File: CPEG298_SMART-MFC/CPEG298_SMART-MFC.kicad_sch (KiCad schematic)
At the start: 4 parts, among them J1 Power, J2 Digital/PWM, J3 Analog, J4 Digital/PWM

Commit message: Lab4_Complete
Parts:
- added C1: C_Polarized_US, Capacitor_THT:CP_Radial_D6.3mm_P2.50mm, symbol Device:C_Polarized_US
- added R1: 1000, Resistor_THT:R_Axial_DIN0207_L6.3mm_D2.5mm_P10.16mm_Horizontal, symbol Device:R_US
- added R2: 2000, Resistor_THT:R_Axial_DIN0207_L6.3mm_D2.5mm_P10.16mm_Horizontal, symbol Device:R_US
- added U1: ESP8266-01/ESP-01, ESP8266-01_ESP-01:XCVR_ESP8266-01_ESP-01, symbol ESP8266-01_ESP-01:ESP8266-01/ESP-01
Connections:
- net *10: now also U1.5 (TXD)
- net *11: now also R1.1
- net +5V: now also C1.1
- net GND: now also C1.2, R2.2, U1.1 (GND)
- new net: R1.2, R2.1, U1.4 (RXD)
- new net +3.3V: U1.6 (EN), U1.8 (VCC)

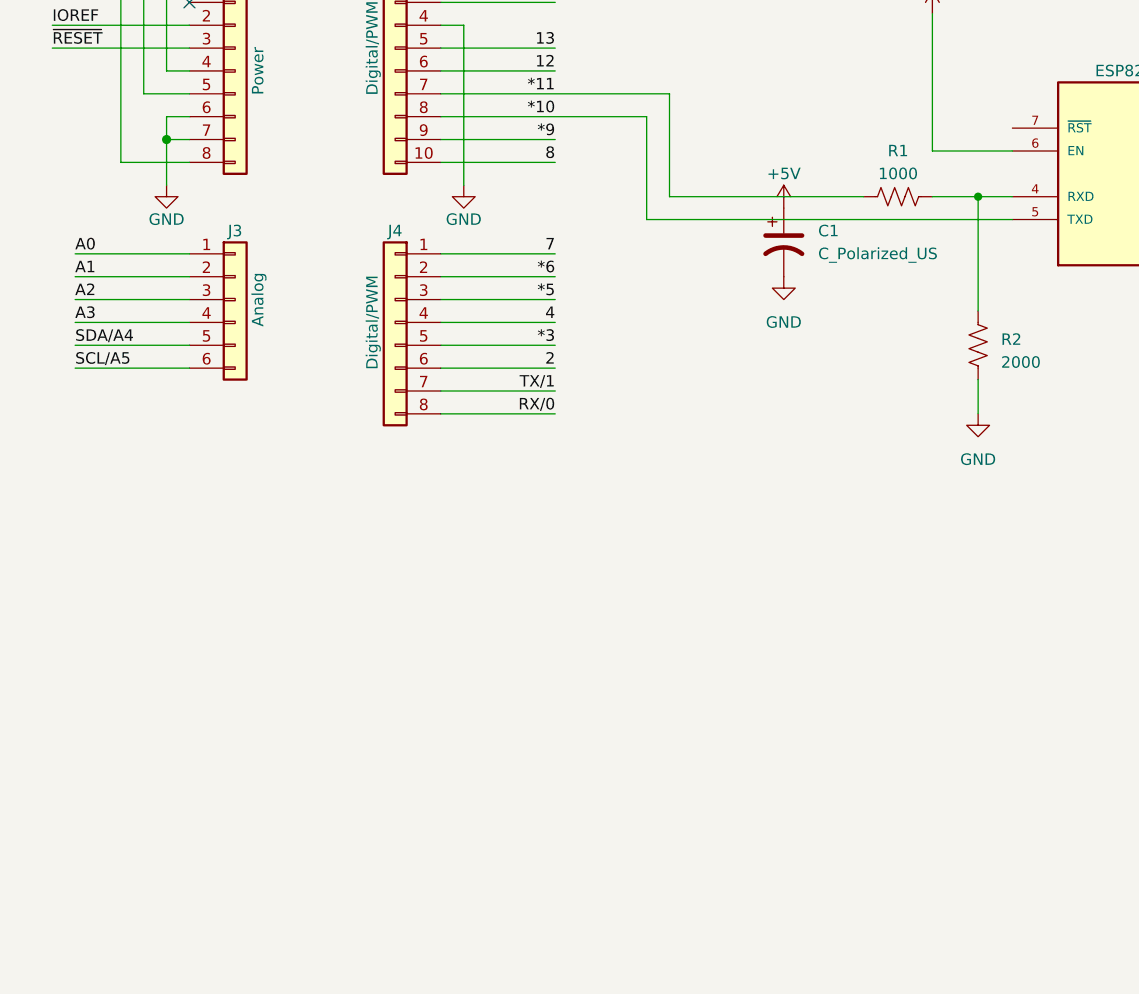
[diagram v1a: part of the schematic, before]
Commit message: Lab5
-Added Grove Connectors
-Rewiring
-3D STEP Files
-New Libraries
*SEEED, Digikey
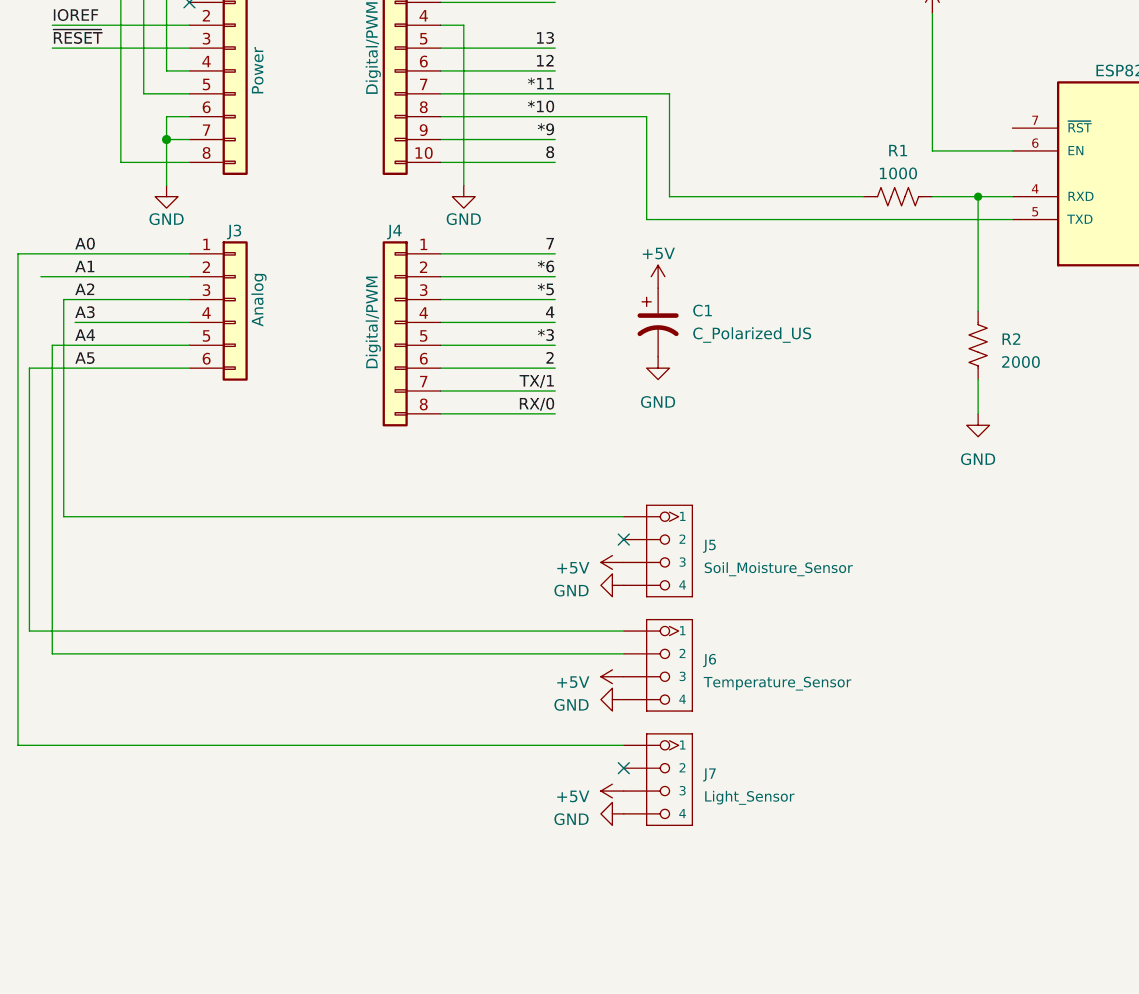
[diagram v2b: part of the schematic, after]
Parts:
- added J5: Soil_Moisture_Sensor, OPL_Connector:HW4-2.0, symbol OPL_Connector:GROVE-CONNECTOR-DIP_4P-2.0_
- added J6: Temperature_Sensor, OPL_Connector:HW4-2.0, symbol OPL_Connector:GROVE-CONNECTOR-DIP_4P-2.0_
- added J7: Light_Sensor, OPL_Connector:HW4-2.0, symbol OPL_Connector:GROVE-CONNECTOR-DIP_4P-2.0_
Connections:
- net +5V: now also J5.3, J6.3, J7.3
- net A0: now also J7.1
- net A2: now also J5.1
- net GND: now also J5.4, J6.4, J7.4
- net SCL/A5: no longer J3.6 (Pin_6)
- net SDA/A4: no longer J3.5 (Pin_5)
- new net A4: J3.5 (Pin_5), J6.2
- new net A5: J3.6 (Pin_6), J6.1
- no-connect marks 1 -> 3
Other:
- moved on the sheet: C1

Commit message: KiCad Components and Software
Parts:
- added C2: C_Polarized_US, Capacitor_THT:CP_Radial_D6.3mm_P2.50mm, symbol Device:C_Polarized_US
- added D1: Soil Moisture Threshold, LED_THT:LED_D5.0mm, symbol Device:LED
- added J8: LCD, OPL_Connector:HW4-2.0, symbol OPL_Connector:GROVE-CONNECTOR-DIP_4P-2.0_
- added R3: R, Resistor_THT:R_Axial_DIN0207_L6.3mm_D2.5mm_P10.16mm_Horizontal, symbol Device:R_US
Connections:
- net +3.3V: now also C2.1
- net +5V: now also J8.3
- net 7: now also R3.1
- net GND: now also C2.2, D1.2 (A), J8.4
- net SCL/A5: now also J8.1
- net SDA/A4: now also J8.2
- new net: D1.1 (K), R3.2
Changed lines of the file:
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@@
     (stroke (width 0) (type solid))
   )
-  (wire (pts (xy 62.23 26.67) (xy 74.93 26.67))
+  (wire (pts (xy 62.23 26.67) (xy 92.71 26.67))
     (stroke (width 0) (type solid))
   )
@@
     (stroke (width 0) (type solid))
   )
+  (wire (pts (xy 82.55 59.69) (xy 82.55 86.36))
+    (stroke (width 0) (type default))
+  )
   (wire (pts (xy 62.23 36.83) (xy 74.93 36.83))
     (stroke (width 0) (type solid))
@@
     (stroke (width 0) (type solid))
   )
-  (wire (pts (xy 62.23 59.69) (xy 74.93 59.69))
+  (wire (pts (xy 62.23 59.69) (xy 82.55 59.69))
     (stroke (width 0) (type solid))
   )
@@
     (stroke (width 0) (type default))
   )
+  (wire (pts (xy 82.55 86.36) (xy 135.89 86.36))
+    (stroke (width 0) (type default))
+  )
   (wire (pts (xy 161.29 58.42) (xy 168.91 58.42))
     (stroke (width 0) (type default))
   )
-  (wire (pts (xy 62.23 29.21) (xy 74.93 29.21))
+  (wire (pts (xy 62.23 29.21) (xy 92.71 29.21))
     (stroke (width 0) (type solid))
   )
@@
     )
   )
+  (symbol (lib_name "+5V_1") (lib_id "power:+5V") (at 92.71 31.75 90) (unit 1)
+    (in_bom yes) (on_board yes) (dnp no) (fields_autoplaced)
+    (property "Reference" "#PWR022" (at 96.52 31.75 0)
+      (effects (font (size 1.27 1.27)) hide)
+    )
+    (property "Value" "+5V" (at 88.9 32.385 90)
+      (effects (font (size 1.27 1.27)) (justify left))
+    )
+    (property "Footprint" "" (at 92.71 31.75 0)
+      (effects (font (size 1.27 1.27)) hide)
+    )
+    (property "Datasheet" "" (at 92.71 31.75 0)
+      (effects (font (size 1.27 1.27)) hide)
+    )
+    (pin "1")
+    (instances
+      (project "CPEG298_SMART-MFC"
+        (path "/e63e39d7-6ac0-4ffd-8aa3-1841a4541b55"
+          (reference "#PWR022") (unit 1)
+        )
+      )
+    )
+  )
   (symbol (lib_id "OPL_Connector:GROVE-CONNECTOR-DIP_4P-2.0_") (at 86.36 118.11 0) (unit 1)
     (in_bom yes) (on_board yes) (dnp no) (fields_autoplaced)
@@
         (path "/e63e39d7-6ac0-4ffd-8aa3-1841a4541b55"
           (reference "J7") (unit 1)
+        )
+      )
+    )
+  )
+  (symbol (lib_name "GND_3") (lib_id "power:GND") (at 135.89 101.6 0) (unit 1)
+    (in_bom yes) (on_board yes) (dnp no) (fields_autoplaced)
+    (property "Reference" "#PWR020" (at 135.89 107.95 0)
+      (effects (font (size 1.27 1.27)) hide)
+    )
+    (property "Value" "GND" (at 135.89 106.68 0)
+      (effects (font (size 1.27 1.27)))
+    )
+    (property "Footprint" "" (at 135.89 101.6 0)
+      (effects (font (size 1.27 1.27)) hide)
+    )
+    (property "Datasheet" "" (at 135.89 101.6 0)
+      (effects (font (size 1.27 1.27)) hide)
+    )
+    (pin "1")
+    (instances
+      (project "CPEG298_SMART-MFC"
+        (path "/e63e39d7-6ac0-4ffd-8aa3-1841a4541b55"
+          (reference "#PWR020") (unit 1)
+        )
+      )
+    )
+  )
+  (symbol (lib_id "OPL_Connector:GROVE-CONNECTOR-DIP_4P-2.0_") (at 96.52 30.48 0) (unit 1)
+    (in_bom yes) (on_board yes) (dnp no) (fields_autoplaced)
+    (property "Reference" "J8" (at 101.6 29.845 0)
+      (effects (font (size 1.143 1.143)) (justify left))
+    )
+    (property "Value" "LCD" (at 101.6 32.385 0)
+      (effects (font (size 1.143 1.143)) (justify left))
+    )
+    (property "Footprint" "OPL_Connector:HW4-2.0" (at 96.52 30.48 0)
+      (effects (font (size 1.27 1.27)) hide)
+    )
+    (property "Datasheet" "" (at 96.52 30.48 0)
+      (effects (font (size 1.27 1.27)) hide)
+    )
+    (property "SKU" "320110033" (at 97.282 26.67 0)
+      (effects (font (size 0.508 0.508)) hide)
+    )
+    (pin "1")
+    (pin "2")
+    (pin "3")
+    (pin "4")
+    (instances
+      (project "CPEG298_SMART-MFC"
+        (path "/e63e39d7-6ac0-4ffd-8aa3-1841a4541b55"
+          (reference "J8") (unit 1)
+        )
+      )
+    )
+  )
+  (symbol (lib_name "GND_1") (lib_id "power:GND") (at 107.95 72.39 0) (unit 1)
+    (in_bom yes) (on_board yes) (dnp no) (fields_autoplaced)
+    (property "Reference" "#PWR019" (at 107.95 78.74 0)
+      (effects (font (size 1.27 1.27)) hide)
+    )
+    (property "Value" "GND" (at 107.95 77.47 0)
+      (effects (font (size 1.27 1.27)))
+    )
+    (property "Footprint" "" (at 107.95 72.39 0)
+      (effects (font (size 1.27 1.27)) hide)
+    )
+    (property "Datasheet" "" (at 107.95 72.39 0)
+      (effects (font (size 1.27 1.27)) hide)
+    )
+    (pin "1")
+    (instances
+      (project "CPEG298_SMART-MFC"
+        (path "/e63e39d7-6ac0-4ffd-8aa3-1841a4541b55"
+          (reference "#PWR019") (unit 1)
         )
       )
@@
     )
   )
+  (symbol (lib_id "power:+3.3V") (at 107.95 64.77 0) (unit 1)
+    (in_bom yes) (on_board yes) (dnp no) (fields_autoplaced)
+    (property "Reference" "#PWR018" (at 107.95 68.58 0)
+      (effects (font (size 1.27 1.27)) hide)
+    )
+    (property "Value" "+3.3V" (at 107.95 60.96 0)
+      (effects (font (size 1.27 1.27)))
+    )
+    (property "Footprint" "" (at 107.95 64.77 0)
+      (effects (font (size 1.27 1.27)) hide)
+    )
+    (property "Datasheet" "" (at 107.95 64.77 0)
+      (effects (font (size 1.27 1.27)) hide)
+    )
+    (pin "1")
+    (instances
+      (project "CPEG298_SMART-MFC"
+        (path "/e63e39d7-6ac0-4ffd-8aa3-1841a4541b55"
+          (reference "#PWR018") (unit 1)
+        )
+      )
+    )
+  )
   (symbol (lib_name "GND_2") (lib_id "power:GND") (at 168.91 67.31 0) (unit 1)
     (in_bom yes) (on_board yes) (dnp no) (fields_autoplaced)
@@
         (path "/e63e39d7-6ac0-4ffd-8aa3-1841a4541b55"
           (reference "#PWR010") (unit 1)
+        )
+      )
+    )
+  )
+  (symbol (lib_name "GND_1") (lib_id "power:GND") (at 92.71 34.29 270) (unit 1)
+    (in_bom yes) (on_board yes) (dnp no) (fields_autoplaced)
+    (property "Reference" "#PWR021" (at 86.36 34.29 0)
+      (effects (font (size 1.27 1.27)) hide)
+    )
+    (property "Value" "GND" (at 88.9 34.925 90)
+      (effects (font (size 1.27 1.27)) (justify right))
+    )
+    (property "Footprint" "" (at 92.71 34.29 0)
+      (effects (font (size 1.27 1.27)) hide)
+    )
+    (property "Datasheet" "" (at 92.71 34.29 0)
+      (effects (font (size 1.27 1.27)) hide)
+    )
+    (pin "1")
+    (instances
+      (project "CPEG298_SMART-MFC"
+        (path "/e63e39d7-6ac0-4ffd-8aa3-1841a4541b55"
+          (reference "#PWR021") (unit 1)
         )
       )
@@
     )
   )
+  (symbol (lib_id "Device:C_Polarized_US") (at 107.95 68.58 0) (unit 1)
+    (in_bom yes) (on_board yes) (dnp no) (fields_autoplaced)
+    (property "Reference" "C2" (at 111.76 67.31 0)
+      (effects (font (size 1.27 1.27)) (justify left))
+    )
+    (property "Value" "C_Polarized_US" (at 111.76 69.85 0)
+      (effects (font (size 1.27 1.27)) (justify left))
+    )
+    (property "Footprint" "Capacitor_THT:CP_Radial_D6.3mm_P2.50mm" (at 107.95 68.58 0)
+      (effects (font (size 1.27 1.27)) hide)
+    )
+    (property "Datasheet" "~" (at 107.95 68.58 0)
+      (effects (font (size 1.27 1.27)) hide)
+    )
+    (pin "1")
+    (pin "2")
+    (instances
+      (project "CPEG298_SMART-MFC"
+        (path "/e63e39d7-6ac0-4ffd-8aa3-1841a4541b55"
+          (reference "C2") (unit 1)
+        )
+      )
+    )
+  )
   (symbol (lib_name "+5V_1") (lib_id "power:+5V") (at 82.55 93.98 90) (unit 1)
     (in_bom yes) (on_board yes) (dnp no) (fields_autoplaced)
@@
         )
       )
+    )
+  )
+  (symbol (lib_id "Device:LED") (at 135.89 97.79 270) (unit 1)
+    (in_bom yes) (on_board yes) (dnp no) (fields_autoplaced)
+    (property "Reference" "D1" (at 138.43 95.5675 90)
+      (effects (font (size 1.27 1.27)) (justify left))
+    )
+    (property "Value" "Soil Moisture Threshold" (at 138.43 98.1075 90)
+      (effects (font (size 1.27 1.27)) (justify left))
+    )
+    (property "Footprint" "LED_THT:LED_D5.0mm" (at 135.89 97.79 0)
+      (effects (font (size 1.27 1.27)) hide)
+    )
+    (property "Datasheet" "~" (at 135.89 97.79 0)
+      (effects (font (size 1.27 1.27)) hide)
+    )
+    (pin "1")
+    (pin "2")
+    (instances
+      (project "CPEG298_SMART-MFC"
+        (path "/e63e39d7-6ac0-4ffd-8aa3-1841a4541b55"
+          (reference "D1") (unit 1)
+        )
+      )
+    )
+  )
+  (symbol (lib_id "Device:R_US") (at 135.89 90.17 0) (unit 1)
+    (in_bom yes) (on_board yes) (dnp no) (fields_autoplaced)
+    (property "Reference" "R3" (at 138.43 89.535 0)
+      (effects (font (size 1.27 1.27)) (justify left))
+    )
+    (property "Value" "R" (at 138.43 92.075 0)
+      (effects (font (size 1.27 1.27)) (justify left))
+    )
+    (property "Footprint" "Resistor_THT:R_Axial_DIN0207_L6.3mm_D2.5mm_P10.16mm_Horizontal" (at 136.906 90.424 90)
+      (effects (font (size 1.27 1.27)) hide)
+    )
+    (property "Datasheet" "~" (at 135.89 90.17 0)
+      (effects (font (size 1.27 1.27)) hide)
+    )
+    (pin "1")
+    (pin "2")
+    (instances
+      (project "CPEG298_SMART-MFC"
+        (path "/e63e39d7-6ac0-4ffd-8aa3-1841a4541b55"
+          (reference "R3") (unit 1)
+        )
+      )
